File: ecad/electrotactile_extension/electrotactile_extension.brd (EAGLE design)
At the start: 80 x 38.4 mm, 218 parts, among them IC1 DRV8662, J1 VERT MALE 2.54MM, J2 VERT MALE 2.54MM, J3 VERT MALE 2.54MM, J4 VERT MALE 2.54MM, J5 VERT MALE 2.54MM, J6 PTH VERT MALE, J7 PTH VERT MALE, J8 PTH VERT MALE, J9 PTH VERT MALE, SW2 25mA/24V

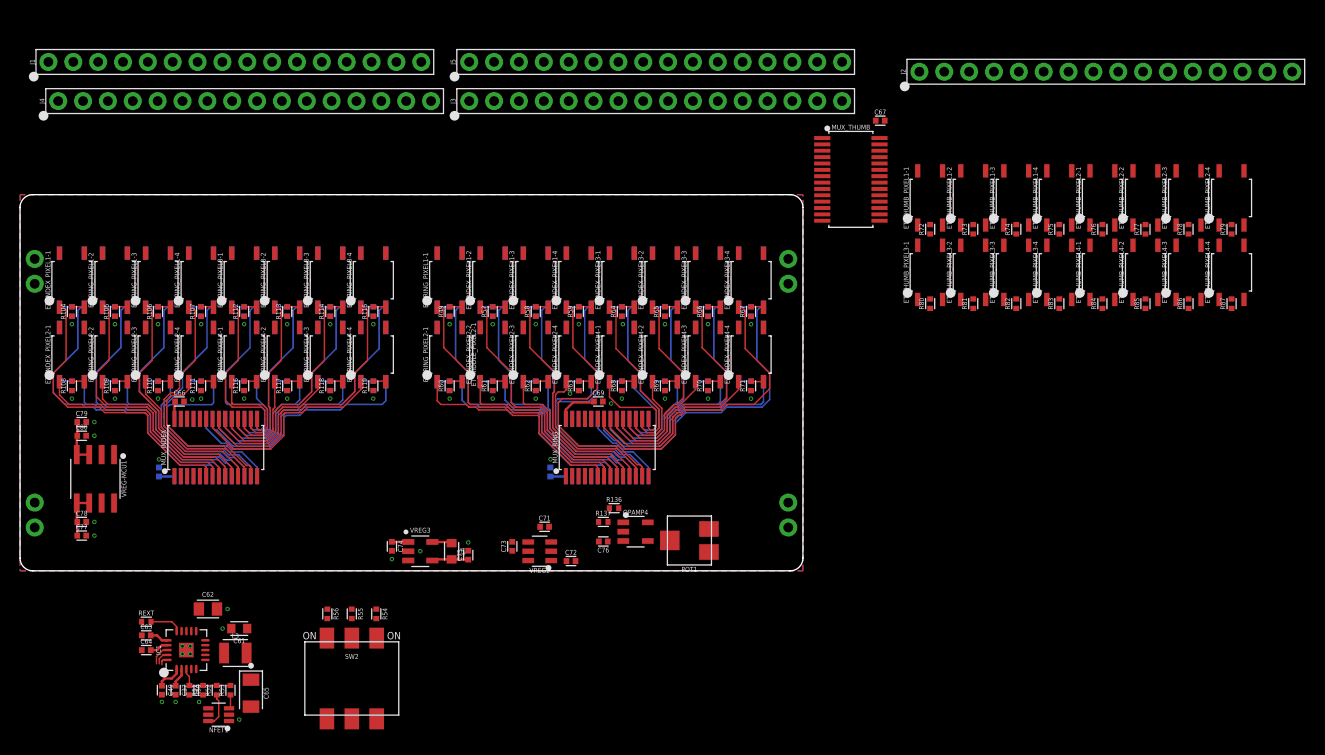
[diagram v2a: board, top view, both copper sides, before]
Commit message: Create PCA9685Servo library.  Touch up Touch Glove PCB.  Major work completed on ET Extension.
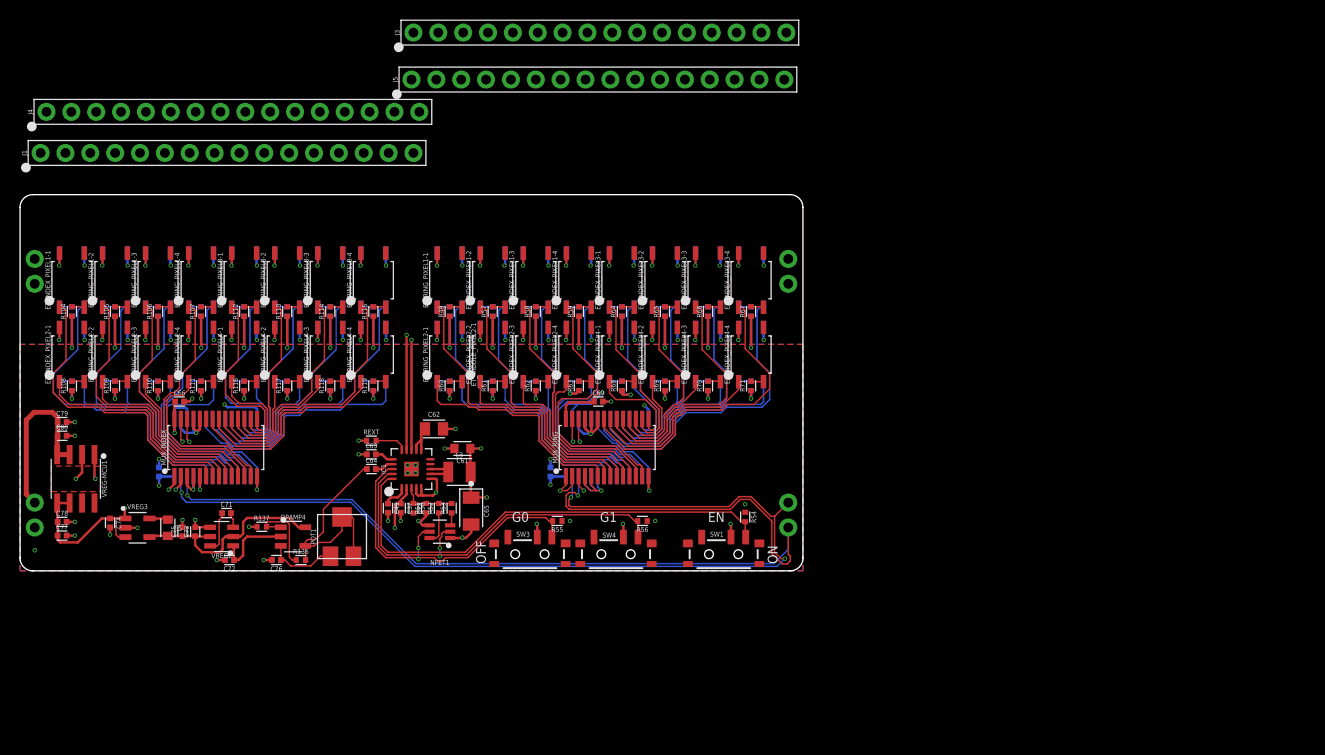
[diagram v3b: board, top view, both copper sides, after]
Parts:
- removed C67: 0.1uF/50V, _capacitors:CAPC1005X55_SMD-0402
- removed ET_THUMB_PIXEL1-1, ET_THUMB_PIXEL1-2, ET_THUMB_PIXEL1-3, ET_THUMB_PIXEL1-4, ET_THUMB_PIXEL2-1, ET_THUMB_PIXEL2-2, ET_THUMB_PIXEL2-3, ET_THUMB_PIXEL2-4, ET_THUMB_PIXEL3-1, ET_THUMB_PIXEL3-2, ET_THUMB_PIXEL3-3, ET_THUMB_PIXEL3-4, ET_THUMB_PIXEL4-1, ET_THUMB_PIXEL4-2, ET_THUMB_PIXEL4-3, ET_THUMB_PIXEL4-4: SPST-NO 170mA 250V, _relay:SOP254P609X203-4
- removed J2: VERT MALE 2.54MM, _connectors:HDRV16W64P254_1X16_4064X254X838B
- removed MUX_THUMB: PCA9685, _special:SOP65P650X110-28
- removed R72, R73, R74, R75, R76, R77, R78, R79, R80, R81, R82, R83, R84, R85, R86, R87: 1K, _resistors:RESC1005X35_SMD-0402
- removed SW2: 25mA/24V, _switches:SW_SLIDE_ARRAY-3_L9.6-W7.5-H4.5
- added SW1, SW3, SW4: 300mA/4V, _switches:SW_SLIDE_SPDT_RA_SMD_4V_300MA_6.7L-2.6W
- moved R54 39.0 mm to (34.1, 5.50)
- moved POT1 35.5 mm to (-7.10, 3.50), turned to 0 degrees
- moved OPAMP4 35.0 mm to (-12.1, 3.50)
- moved R137 34.9 mm to (-15.3, 4.50)
- moved C72 34.9 mm to (-18.6, 1.10), turned to 180 degrees
- moved R56 33.6 mm to (23.6, 5.10), turned to 180 degrees
- moved C76 33.5 mm to (-13.8, 1.10)
- moved VREG2 32.5 mm to (-19.4, 3.50)
- moved C71 32.5 mm to (-18.9, 5.90)
- moved R136 32.4 mm to (-11.3, 1.10)
- moved C73 32.4 mm to (-22.1, 4.00)
- moved C49 29.7 mm to (-2.40, 6.40)
- moved C37 29.6 mm to (-1.10, 6.40)
- moved C62 29.5 mm to (2.30, 14.5)
- moved C63 29.5 mm to (-4.10, 11.9)
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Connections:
- removed net N$58: ET_THUMB_PIXEL1-1.2, R72.2
- removed net N$7: VREG3.3
- removed net N$74: ET_THUMB_PIXEL1-2.2, R73.2
- removed net N$75: ET_THUMB_PIXEL1-3.2, R74.2
- removed net N$76: ET_THUMB_PIXEL1-4.2, R75.2
- removed net N$77: ET_THUMB_PIXEL2-1.2, R76.2
- removed net N$78: ET_THUMB_PIXEL2-2.2, R77.2
- removed net N$79: ET_THUMB_PIXEL2-3.2, R78.2
- removed net N$80: ET_THUMB_PIXEL2-4.2, R79.2
- removed net N$81: ET_THUMB_PIXEL3-1.2, R80.2
- removed net N$82: ET_THUMB_PIXEL3-2.2, R81.2
- removed net N$83: ET_THUMB_PIXEL3-3.2, R82.2
- removed net N$84: ET_THUMB_PIXEL3-4.2, R83.2
- removed net N$85: ET_THUMB_PIXEL4-1.2, R84.2
- removed net N$86: ET_THUMB_PIXEL4-2.2, R85.2
- removed net N$87: ET_THUMB_PIXEL4-3.2, R86.2
- removed net N$88: ET_THUMB_PIXEL4-4.2, R87.2
- removed net NGND: J8.1, J8.2
- removed net THUMB_IN1-1: ET_THUMB_PIXEL1-1.1, MUX_THUMB.6
- removed net THUMB_IN1-2: ET_THUMB_PIXEL1-2.1, MUX_THUMB.7
- removed net THUMB_IN1-3: ET_THUMB_PIXEL1-3.1, MUX_THUMB.8
- removed net THUMB_IN1-4: ET_THUMB_PIXEL1-4.1, MUX_THUMB.9
- removed net THUMB_IN2-1: ET_THUMB_PIXEL2-1.1, MUX_THUMB.10
- removed net THUMB_IN2-2: ET_THUMB_PIXEL2-2.1, MUX_THUMB.11
- removed net THUMB_IN2-3: ET_THUMB_PIXEL2-3.1, MUX_THUMB.12
- removed net THUMB_IN2-4: ET_THUMB_PIXEL2-4.1, MUX_THUMB.13
- removed net THUMB_IN3-1: ET_THUMB_PIXEL3-1.1, MUX_THUMB.15
- removed net THUMB_IN3-2: ET_THUMB_PIXEL3-2.1, MUX_THUMB.16
- removed net THUMB_IN3-3: ET_THUMB_PIXEL3-3.1, MUX_THUMB.17
- removed net THUMB_IN3-4: ET_THUMB_PIXEL3-4.1, MUX_THUMB.18
- removed net THUMB_IN4-1: ET_THUMB_PIXEL4-1.1, MUX_THUMB.19
- removed net THUMB_IN4-2: ET_THUMB_PIXEL4-2.1, MUX_THUMB.20
- removed net THUMB_IN4-3: ET_THUMB_PIXEL4-3.1, MUX_THUMB.21
- removed net THUMB_IN4-4: ET_THUMB_PIXEL4-4.1, MUX_THUMB.22
- removed net THUMB_OUT1-1: ET_THUMB_PIXEL1-1.3
- removed net THUMB_OUT1-2: ET_THUMB_PIXEL1-2.3
- removed net THUMB_OUT1-3: ET_THUMB_PIXEL1-3.3
- removed net THUMB_OUT1-4: ET_THUMB_PIXEL1-4.3
- removed net THUMB_OUT2-1: ET_THUMB_PIXEL2-1.3
- removed net THUMB_OUT2-2: ET_THUMB_PIXEL2-2.3
- removed net THUMB_OUT2-3: ET_THUMB_PIXEL2-3.3
- removed net THUMB_OUT2-4: ET_THUMB_PIXEL2-4.3
- removed net THUMB_OUT3-1: ET_THUMB_PIXEL3-1.3
- removed net THUMB_OUT3-2: ET_THUMB_PIXEL3-2.3
- removed net THUMB_OUT3-3: ET_THUMB_PIXEL3-3.3
- removed net THUMB_OUT3-4: ET_THUMB_PIXEL3-4.3
- removed net THUMB_OUT4-1: ET_THUMB_PIXEL4-1.3
- removed net THUMB_OUT4-2: ET_THUMB_PIXEL4-2.3
- removed net THUMB_OUT4-3: ET_THUMB_PIXEL4-3.3
- removed net THUMB_OUT4-4: ET_THUMB_PIXEL4-4.3
- removed net VCC: C66.1, C67.1, C68.1, C69.1, C70.1, MUX_INDEX.28, MUX_MIDDLE.28, MUX_PINKY.28, MUX_RING.28, MUX_THUMB.28
- net 3.3V: now also C66.1, C68.1, C69.1, C70.1, MUX_INDEX.2, MUX_INDEX.28, MUX_MIDDLE.1, MUX_MIDDLE.2, MUX_MIDDLE.28, MUX_PINKY.1, MUX_PINKY.28, MUX_PINKY.3, MUX_RING.28, MUX_RING.3, SW1.2, SW3.2, SW4.2, VREG3.3; no longer SW2.P1, SW2.P2, SW2.P3
- net EN: now also SW1.3; no longer SW2.S3
- net GAIN0: now also SW3.3; no longer SW2.S2
- net GAIN1: now also SW4.3; no longer SW2.S1
- net GND: no longer C67.2, MUX_INDEX.2, MUX_MIDDLE.1, MUX_MIDDLE.2, MUX_PINKY.1, MUX_PINKY.3, MUX_RING.3, MUX_THUMB.1, MUX_THUMB.14, MUX_THUMB.2, MUX_THUMB.23, MUX_THUMB.24, MUX_THUMB.25, MUX_THUMB.3, MUX_THUMB.4, MUX_THUMB.5, R72.1, R73.1, R74.1, R75.1, R76.1, R77.1, R78.1, R79.1, R80.1, R81.1, R82.1, R83.1, R84.1, R85.1, R86.1, R87.1
- net INDEX_OUT1-1: no longer J2.1
- net SCL: no longer MUX_THUMB.26
- net SDA: no longer MUX_THUMB.27
- net V+: no longer ET_THUMB_PIXEL1-1.4, ET_THUMB_PIXEL1-2.4, ET_THUMB_PIXEL1-3.4, ET_THUMB_PIXEL1-4.4, ET_THUMB_PIXEL2-1.4, ET_THUMB_PIXEL2-2.4, ET_THUMB_PIXEL2-3.4, ET_THUMB_PIXEL2-4.4, ET_THUMB_PIXEL3-1.4, ET_THUMB_PIXEL3-2.4, ET_THUMB_PIXEL3-3.4, ET_THUMB_PIXEL3-4.4, ET_THUMB_PIXEL4-1.4, ET_THUMB_PIXEL4-2.4, ET_THUMB_PIXEL4-3.4, ET_THUMB_PIXEL4-4.4
- net V-: no longer J2.16
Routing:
- net V+: track 0.00 -> 244.5 mm, vias 0 -> 65
- net GND: track 0.00 -> 219.8 mm, vias 49 -> 73
- net SCL: track 0.00 -> 121.4 mm, vias 0 -> 4
- net SDA: track 0.00 -> 115.5 mm, vias 0 -> 5
- net 3.3V: track 8.24 -> 63.1 mm, vias 0 -> 13
- net EN: track 1.00 -> 48.7 mm
- net GAIN1: track 1.52 -> 42.3 mm, vias 0 -> 2
- net GAIN0: track 2.14 -> 35.1 mm, vias 0 -> 2
- net IN+: track 0.00 -> 23.4 mm
- net 1.8V: track 3.73 -> 21.9 mm
- net VBAT: track 4.62 -> 17.6 mm
- net V-: track 0.00 -> 11.8 mm, vias 0 -> 1
- net VCC: track 9.14 -> 0.00 mm
- net N$138: track 0.00 -> 8.61 mm
- net -1.8V: track 0.00 -> 8.13 mm
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- added copper zone on layer 2, net 3.3V
- added copper zone on layer 2, net V+
- added copper zone on layer 15, net V-
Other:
- board text added: "EN"
- board text added: "G0"
- board text added: "G1"
- board text added: "OFF"
- board text added: "ON"

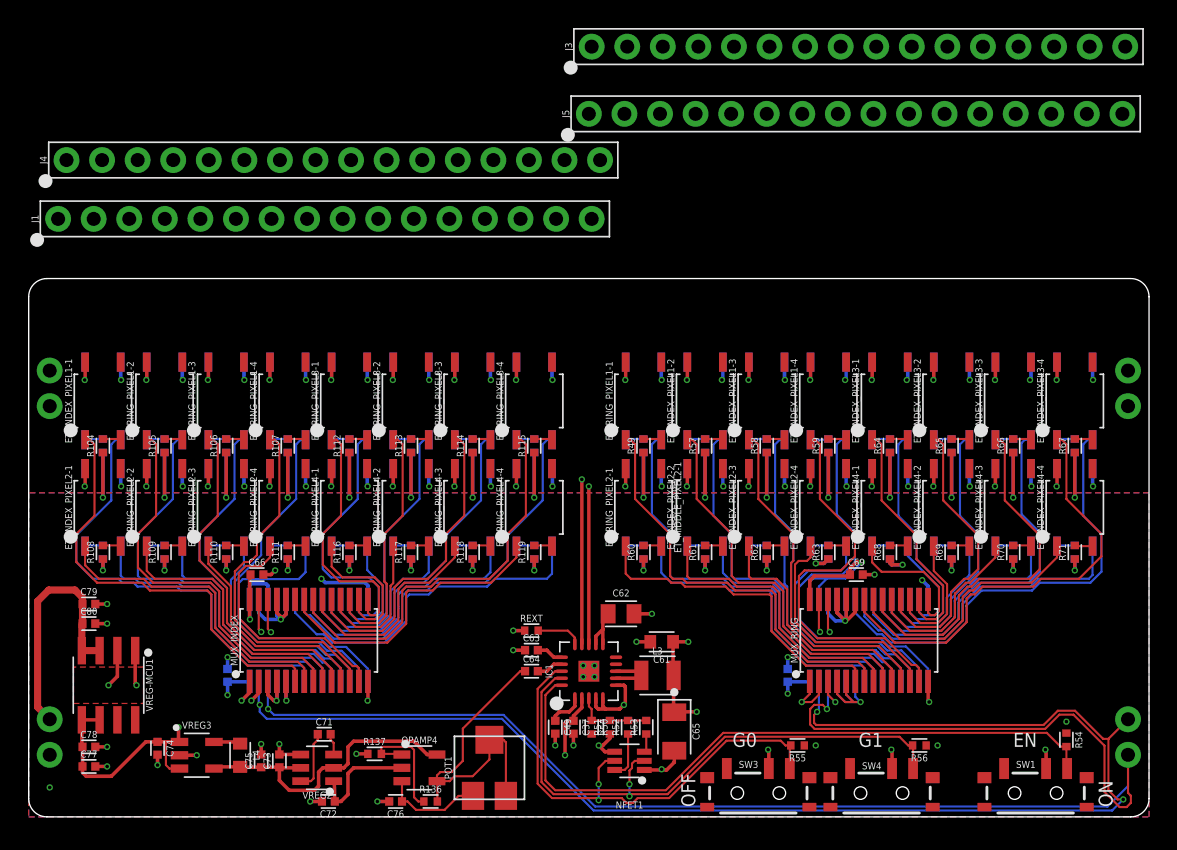
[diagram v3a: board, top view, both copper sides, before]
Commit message: Complete iteration of ET Extension and Touch Glove.  Verify PCA9685Servo library works and made appropriate changes in robotic arm master code.
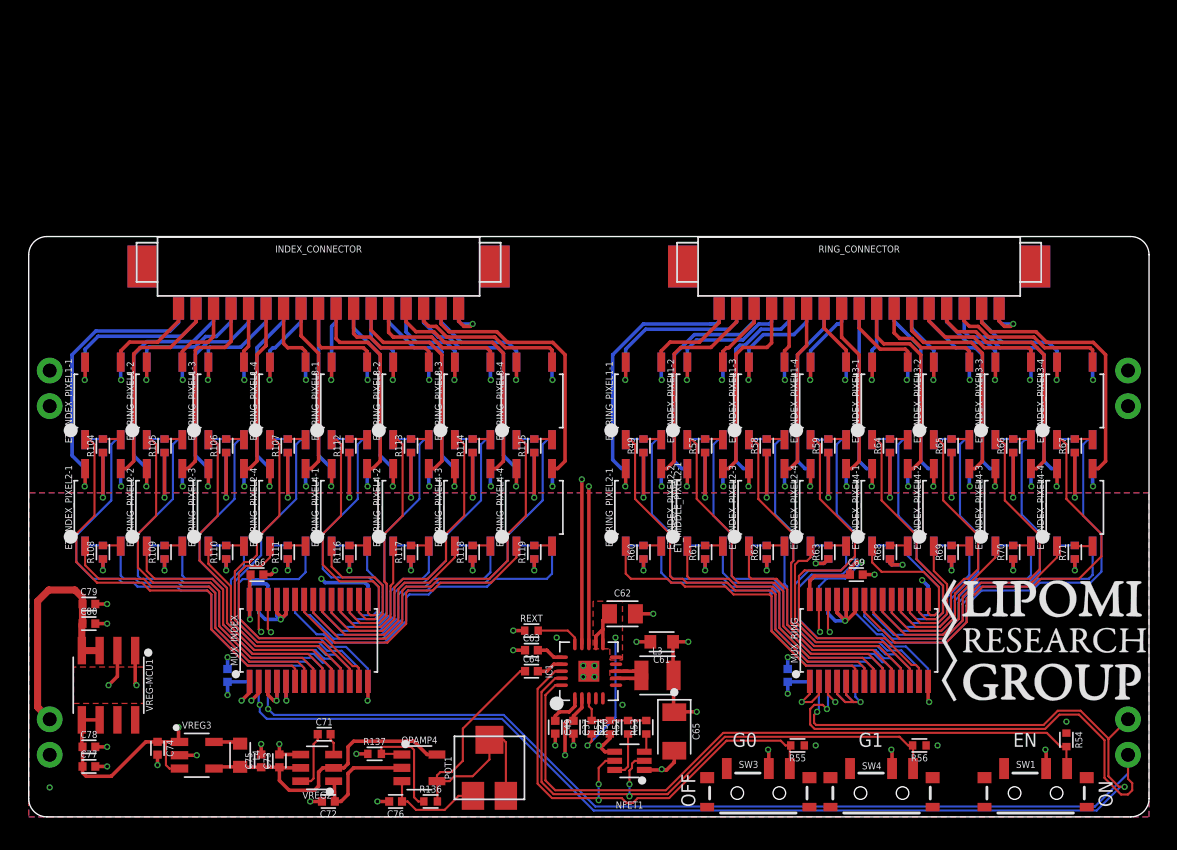
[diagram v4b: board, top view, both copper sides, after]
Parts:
- removed J1, J3, J4, J5: VERT MALE 2.54MM, _connectors:HDRV16W64P254_1X16_4064X254X838B
- added INDEX_CONNECTOR, MIDDLE_CONNECTOR, PINKY_CONNECTOR, RING_CONNECTOR: 1x17 MOLEX SMD RA, _connectors:1X17_MOLEX_0532611771_RA_SMD
- J6, J7, J8, J9: value PTH VERT MALE -> 1x02 PTH VERT FEMALE; device _connectors:HDRV2W64P254_1X2_508X254X838B -> _connectors:HDRVR2W64P254_1X2_558X254X850B
- moved U$2 36.1 mm to (-9.90, 12.4)
- moved U$1 34.4 mm to (32.5, 12.6), flipped to the top
- moved C62 0.10 mm to (2.40, 14.5)
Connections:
- net INDEX_OUT1-1: now also INDEX_CONNECTOR.1; no longer J1.1, J3.1, J4.1, J5.1
- net INDEX_OUT1-2: now also INDEX_CONNECTOR.3
- net INDEX_OUT1-3: now also INDEX_CONNECTOR.5
- net INDEX_OUT1-4: now also INDEX_CONNECTOR.7
- net INDEX_OUT2-1: now also INDEX_CONNECTOR.2
- net INDEX_OUT2-2: now also INDEX_CONNECTOR.4
- net INDEX_OUT2-3: now also INDEX_CONNECTOR.6
- net INDEX_OUT2-4: now also INDEX_CONNECTOR.8
- net INDEX_OUT3-1: now also INDEX_CONNECTOR.9
- net INDEX_OUT3-2: now also INDEX_CONNECTOR.11
- net INDEX_OUT3-3: now also INDEX_CONNECTOR.13
- net INDEX_OUT3-4: now also INDEX_CONNECTOR.15
- net INDEX_OUT4-1: now also INDEX_CONNECTOR.10
- net INDEX_OUT4-2: now also INDEX_CONNECTOR.12
- net INDEX_OUT4-3: now also INDEX_CONNECTOR.14
- net INDEX_OUT4-4: now also INDEX_CONNECTOR.16
- net MIDDLE_OUT1-1: now also MIDDLE_CONNECTOR.16
- net MIDDLE_OUT1-2: now also MIDDLE_CONNECTOR.14
- net MIDDLE_OUT1-3: now also MIDDLE_CONNECTOR.12
- net MIDDLE_OUT1-4: now also MIDDLE_CONNECTOR.10
- net MIDDLE_OUT2-1: now also MIDDLE_CONNECTOR.17
- net MIDDLE_OUT2-2: now also MIDDLE_CONNECTOR.15
- net MIDDLE_OUT2-3: now also MIDDLE_CONNECTOR.13
- net MIDDLE_OUT2-4: now also MIDDLE_CONNECTOR.11
- net MIDDLE_OUT3-1: now also MIDDLE_CONNECTOR.8
- net MIDDLE_OUT3-2: now also MIDDLE_CONNECTOR.6
- net MIDDLE_OUT3-3: now also MIDDLE_CONNECTOR.4
- net MIDDLE_OUT3-4: now also MIDDLE_CONNECTOR.2
- net MIDDLE_OUT4-1: now also MIDDLE_CONNECTOR.9
- net MIDDLE_OUT4-2: now also MIDDLE_CONNECTOR.7
- net MIDDLE_OUT4-3: now also MIDDLE_CONNECTOR.5
- net MIDDLE_OUT4-4: now also MIDDLE_CONNECTOR.3
- net PINKY_OUT1-1: now also PINKY_CONNECTOR.16
- net PINKY_OUT1-2: now also PINKY_CONNECTOR.14
- net PINKY_OUT1-3: now also PINKY_CONNECTOR.12
- net PINKY_OUT1-4: now also PINKY_CONNECTOR.10
- net PINKY_OUT2-1: now also PINKY_CONNECTOR.17
- net PINKY_OUT2-2: now also PINKY_CONNECTOR.15
- net PINKY_OUT2-3: now also PINKY_CONNECTOR.13
- net PINKY_OUT2-4: now also PINKY_CONNECTOR.11
- net PINKY_OUT3-1: now also PINKY_CONNECTOR.8
- net PINKY_OUT3-2: now also PINKY_CONNECTOR.6
- net PINKY_OUT3-3: now also PINKY_CONNECTOR.4
- net PINKY_OUT3-4: now also PINKY_CONNECTOR.2
- net PINKY_OUT4-1: now also PINKY_CONNECTOR.9
- net PINKY_OUT4-2: now also PINKY_CONNECTOR.7
- net PINKY_OUT4-3: now also PINKY_CONNECTOR.5
- net PINKY_OUT4-4: now also PINKY_CONNECTOR.3
- net RING_OUT1-1: now also RING_CONNECTOR.1
- net RING_OUT1-2: now also RING_CONNECTOR.3
- net RING_OUT1-3: now also RING_CONNECTOR.5
- net RING_OUT1-4: now also RING_CONNECTOR.7
- net RING_OUT2-1: now also RING_CONNECTOR.2
- net RING_OUT2-2: now also RING_CONNECTOR.4
- net RING_OUT2-3: now also RING_CONNECTOR.6
- net RING_OUT2-4: now also RING_CONNECTOR.8
- net RING_OUT3-1: now also RING_CONNECTOR.9
- net RING_OUT3-2: now also RING_CONNECTOR.11
- net RING_OUT3-3: now also RING_CONNECTOR.13
- net RING_OUT3-4: now also RING_CONNECTOR.15
- net RING_OUT4-1: now also RING_CONNECTOR.10
- net RING_OUT4-2: now also RING_CONNECTOR.12
- net RING_OUT4-3: now also RING_CONNECTOR.14
- net RING_OUT4-4: now also RING_CONNECTOR.16
- net V-: now also INDEX_CONNECTOR.17, MIDDLE_CONNECTOR.1, PINKY_CONNECTOR.1, RING_CONNECTOR.17; no longer J1.16, J3.16, J4.16, J5.16
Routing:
- net INDEX_OUT4-4: track 0.00 -> 19.6 mm
- net RING_OUT4-4: track 0.00 -> 19.5 mm
- net MIDDLE_OUT2-1: track 0.00 -> 18.2 mm
- net PINKY_OUT2-1: track 0.00 -> 18.1 mm
- net INDEX_OUT4-3: track 0.00 -> 17.7 mm
- net RING_OUT4-3: track 0.00 -> 17.6 mm
- net MIDDLE_OUT4-4: track 0.00 -> 16.8 mm
- net MIDDLE_OUT2-2: track 0.00 -> 16.3 mm
- net PINKY_OUT4-4: track 0.00 -> 16.2 mm
- net RING_OUT4-2: track 0.00 -> 16.1 mm
- net PINKY_OUT2-2: track 0.00 -> 16.1 mm
- net INDEX_OUT4-2: track 0.00 -> 16.1 mm
- net RING_OUT2-1: track 0.00 -> 15.2 mm
- net INDEX_OUT2-1: track 0.00 -> 15.2 mm
- net MIDDLE_OUT2-3: track 0.00 -> 14.7 mm
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- added copper zone on layer 1, net N$42
- added copper zone on layer 1, net N$44
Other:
- board size 80 x 38.4 mm -> 80 x 41.4 mm
